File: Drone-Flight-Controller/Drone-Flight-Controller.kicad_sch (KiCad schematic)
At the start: 60 parts, among them J1 Screw_Terminal_01x02, J10 TestPoint, J2 Raspberry_Pi_4, J3 USB_B_Micro, J4 Conn_ARM_SWD_TagConnect_TC203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, J5 TestPoint, J6 TestPoint, J7 TestPoint, J8 TestPoint, J9 TestPoint, U1 LMR51430, U2 USBLC6-2SC6, U3 MPU-9150, U4 BMP280, U5 STM32F413ZHTx, U6 XTSD08G, Y1 16MHz

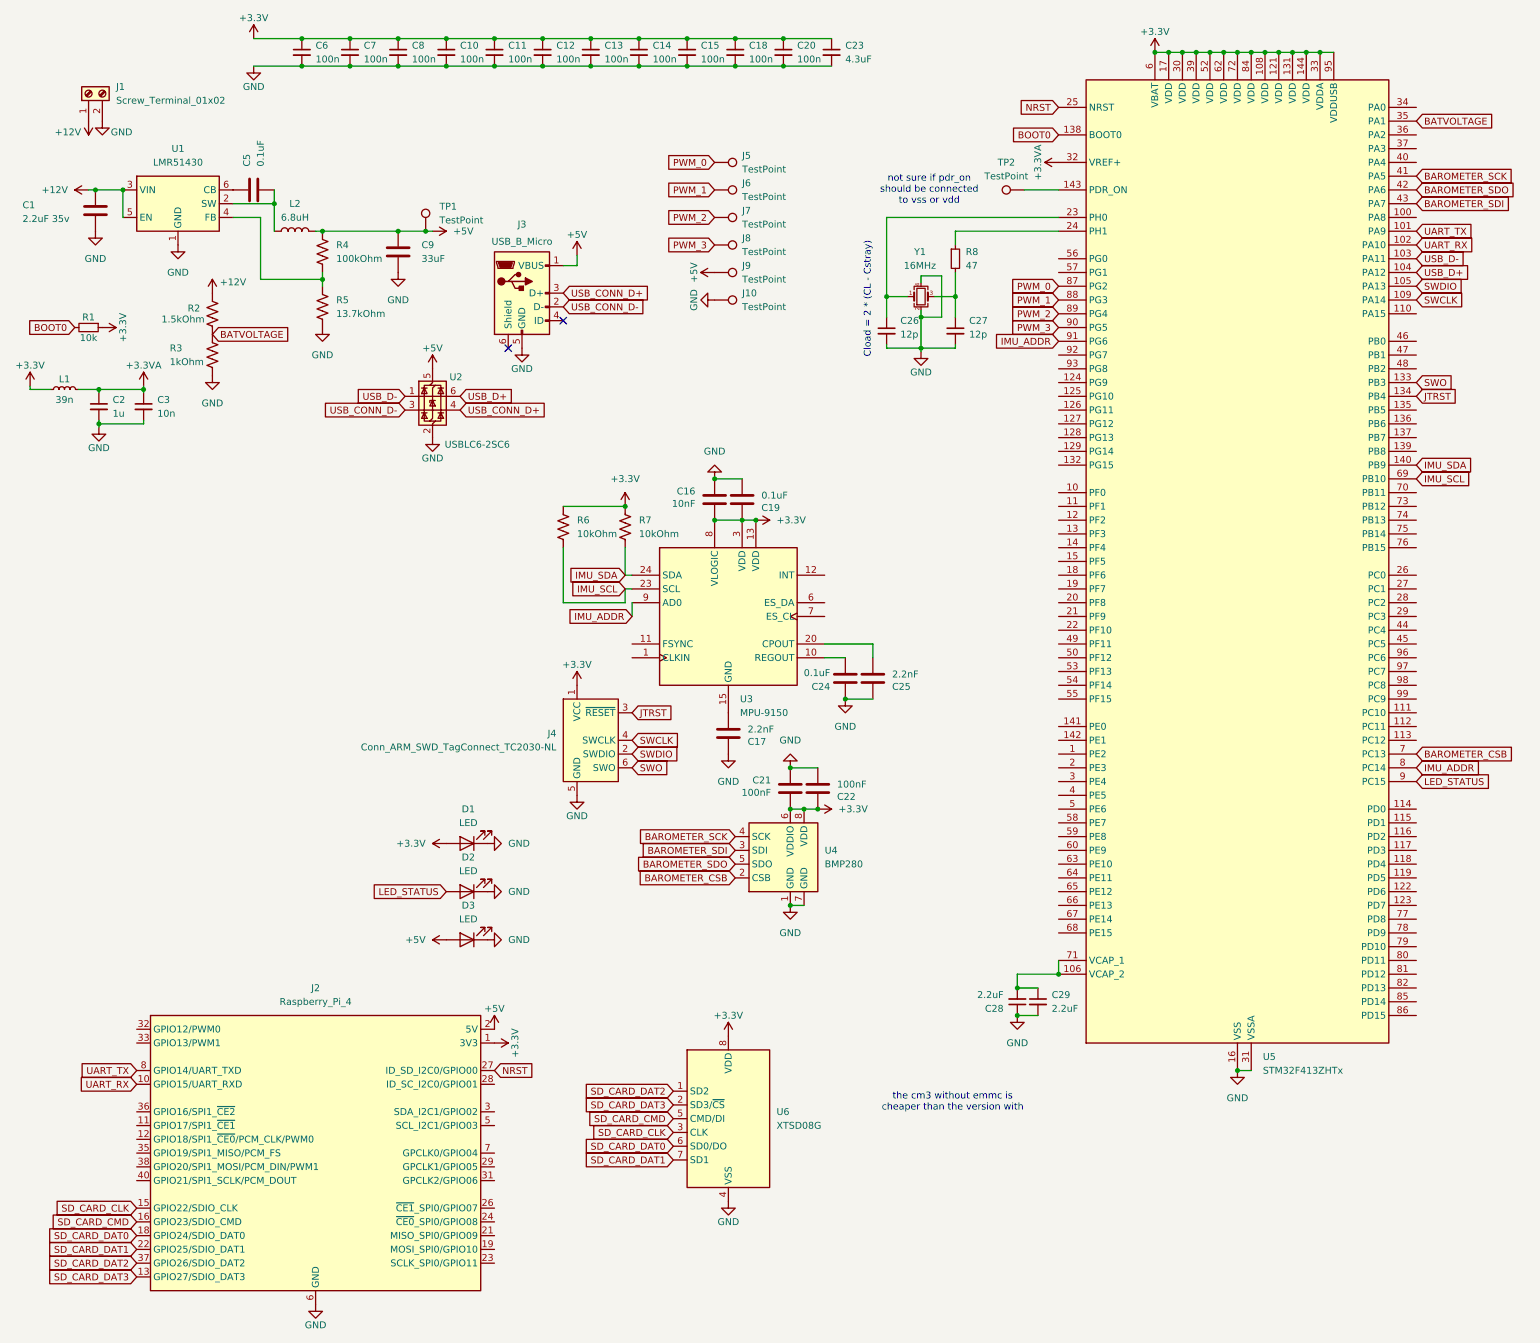
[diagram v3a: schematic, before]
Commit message: remove stm32
processing will be done on the rpi now
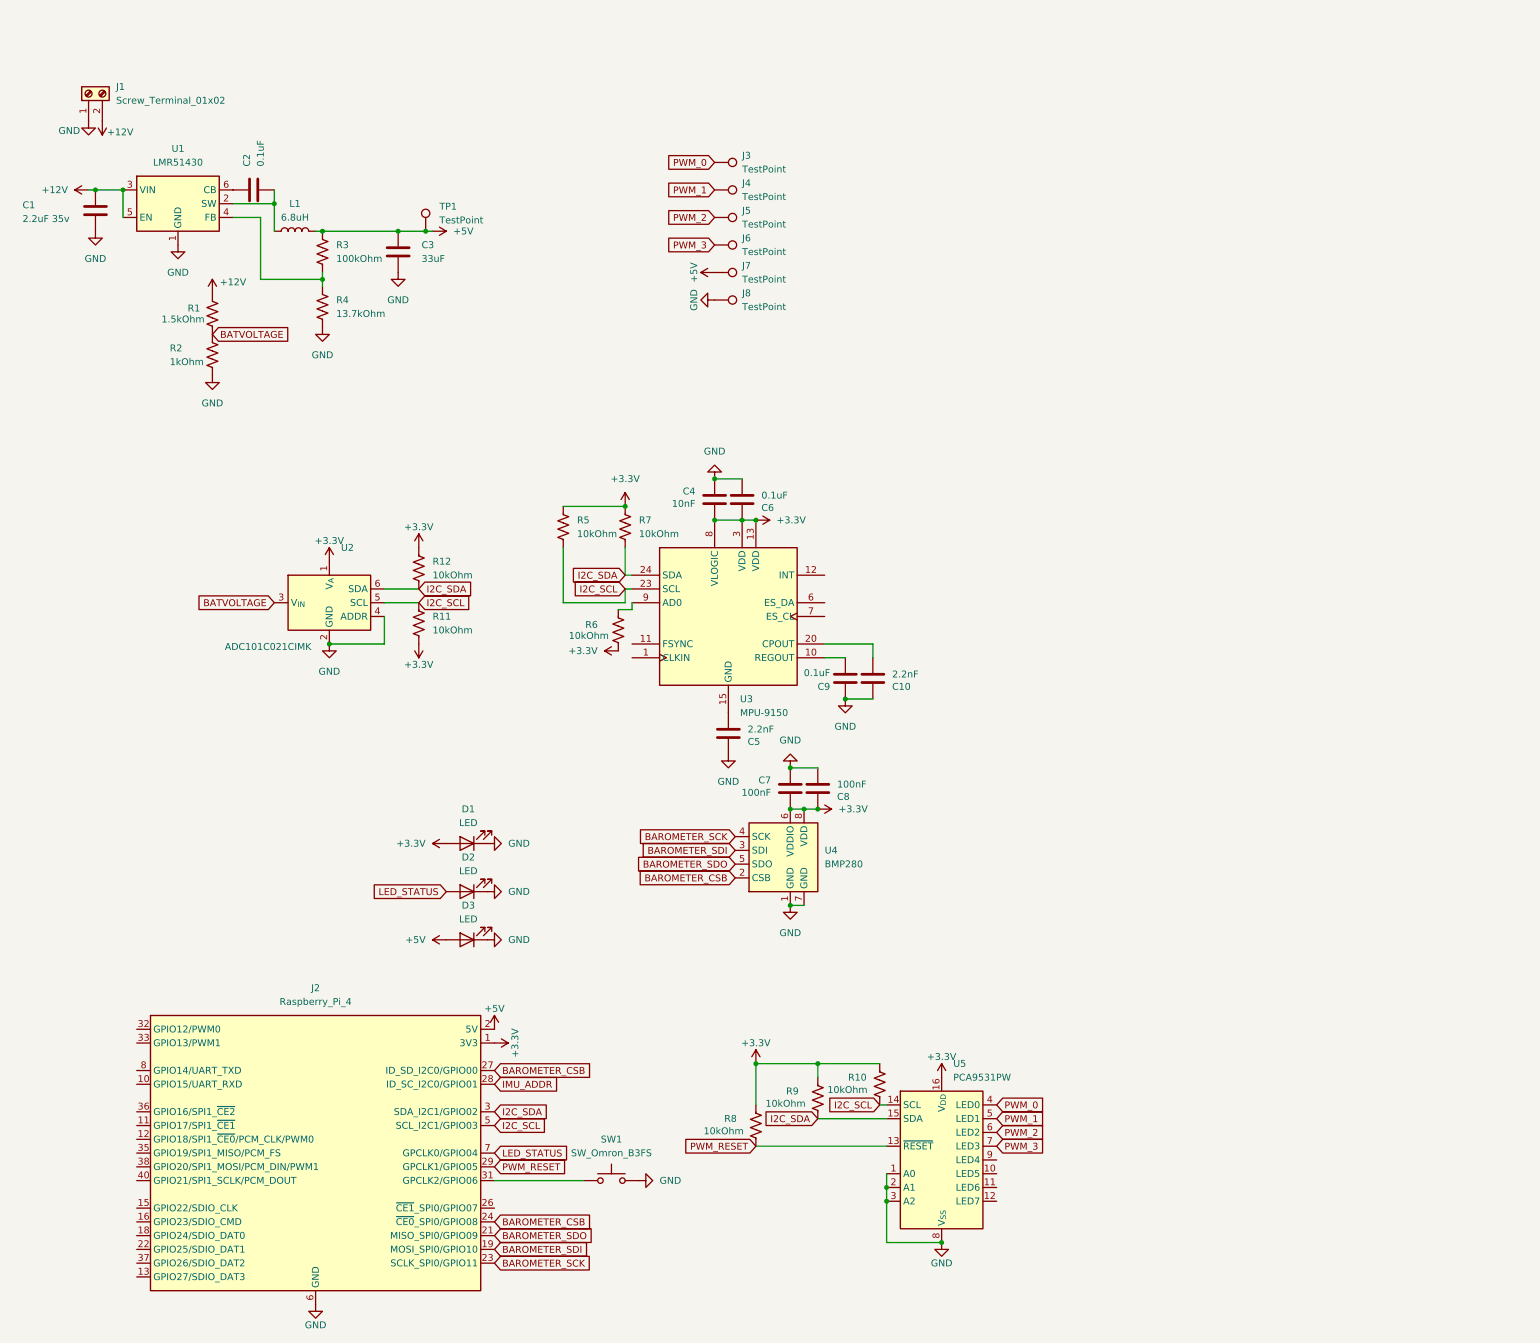
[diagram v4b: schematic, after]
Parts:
- removed C10, C11, C12, C13, C14, C15, C18, C20, C6, C7, C8: 100n, Capacitor_SMD:C_0402_1005Metric, symbol Device:C_Small
- removed C2: 1u, Capacitor_SMD:C_0402_1005Metric, symbol Device:C_Small
- removed C23: 4.3uF, Capacitor_SMD:C_0402_1005Metric, symbol Device:C_Small
- removed C26, C27: 12p, Capacitor_SMD:C_0402_1005Metric, symbol Device:C_Small
- removed C28, C29: 2.2uF, Capacitor_SMD:C_0402_1005Metric, symbol Device:C_Small
- removed C3: 10n, Capacitor_SMD:C_0402_1005Metric, symbol Device:C_Small
- removed J3: USB_B_Micro, Connector_USB:USB_Mini-B_Lumberg_2486_01_Horizontal, symbol Connector:USB_B_Micro
- removed J4: Conn_ARM_SWD_TagConnect_TC2030-NL, Connector:Tag-Connect_TC2030-IDC-NL_2x03_P1.27mm_Vertical, symbol Connector:Conn_ARM_SWD_TagConnect_TC2030-NL
- removed L1: 39n, Inductor_SMD:L_0402_1005Metric, symbol Device:L_Small
- removed R1: 10k, Resistor_SMD:R_0402_1005Metric, symbol Device:R_Small
- removed R8: 47, Resistor_SMD:R_0402_1005Metric, symbol Device:R_Small
- removed TP2: TestPoint, TestPoint:TestPoint_Pad_D1.0mm, symbol Connector:TestPoint
- removed U2: USBLC6-2SC6, Package_TO_SOT_SMD:SOT-23-6, symbol Power_Protection:USBLC6-2SC6
- removed U5: STM32F413ZHTx, Package_QFP:LQFP-144_20x20mm_P0.5mm, symbol MCU_ST_STM32F4:STM32F413ZHTx
- removed U6: XTSD08G, Package_LGA:LGA-8_8x6mm_P1.27mm, symbol Memory_Flash:XTSD08G
- removed Y1: 16MHz, Crystal:Crystal_SMD_3225-4Pin_3.2x2.5mm, symbol Device:Crystal_GND24_Small
- added R10, R11, R12, R6, R8, R9: 10kOhm, Resistor_SMD:R_0402_1005Metric, symbol Device:R_US
- added SW1: SW_Omron_B3FS, Button_Switch_SMD:SW_SPST_Omron_B3FS-100xP, symbol Switch:SW_Omron_B3FS
- added U2: ADC101C021CIMK, Package_TO_SOT_SMD:SOT-23-6, symbol Analog_ADC:ADC101C021CIMK
- added U5: PCA9531PW, Package_SO:TSSOP-16_4.4x5mm_P0.65mm, symbol Driver_LED:PCA9531PW
- C3: renamed from C9; footprint Capacitor_SMD:C_0504_1310Metric -> Capacitor_SMD:C_Elec_5x5.4
- renumbered C25 to C10, C5 to C2, C16 to C4, C17 to C5, C19 to C6, C21 to C7, C22 to C8, C24 to C9, J5 to J3, J6 to J4, J7 to J5, J8 to J6, J9 to J7, J10 to J8, L2 to L1, R2 to R1, R3 to R2, R4 to R3, R5 to R4, R6 to R5
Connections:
- net IMU_SCL is gone; now on net I2C_SCL: R5.2, U3.23 (SCL)
- net IMU_SDA is gone; now on net I2C_SDA: R7.2, U3.24 (SDA)
- net NRST is gone; now on net BAROMETER_CSB: J2.27 (ID_SD_I2C0/GPIO00)
- net +12V: now also J1.2 (Pin_2); no longer J1.1 (Pin_1)
- net +3.3V: now also R10.1, R11.2, R12.1, R6.2, R8.1, R9.1, U2.1 (V_{A}), U5.16 (V_{DD})
- net BAROMETER_CSB: now also J2.24 (~{CE0}_SPI0/GPIO08)
- net BAROMETER_SCK: now also J2.23 (SCLK_SPI0/GPIO11)
- net BAROMETER_SDI: now also J2.19 (MOSI_SPI0/GPIO10)
- net BAROMETER_SDO: now also J2.21 (MISO_SPI0/GPIO09)
- net BATVOLTAGE: now also U2.3 (V_{IN})
- net GND: now also J1.1 (Pin_1), SW1.2, U2.2 (GND), U2.4 (ADDR), U5.1 (A0), U5.2 (A1), U5.3 (A2), U5.8 (V_{SS}); no longer J1.2 (Pin_2)
- net IMU_ADDR: now also J2.28 (ID_SC_I2C0/GPIO01); no longer U3.9 (AD0)
- net LED_STATUS: now also J2.7 (GPCLK0/GPIO04)
- net PWM_0: now also U5.4 (LED0)
- net PWM_1: now also U5.5 (LED1)
- net PWM_2: now also U5.6 (LED2)
- net PWM_3: now also U5.7 (LED3)
- net PWM_RESET: now reaches J2.29 (GPCLK1/GPIO05)
- net PWM_RESET: now also R8.2, U5.13 (~{RESET})
- net I2C_SDA: now reaches J2.3 (SDA_I2C1/GPIO02)
- net I2C_SDA: now also R12.2, R9.2, U2.6 (SDA), U5.15 (SDA)
- net at J2.31 (GPCLK2/GPIO06): now also SW1.1
- net I2C_SCL: now reaches J2.5 (SCL_I2C1/GPIO03)
- net I2C_SCL: now also R10.2, R11.1, U2.5 (SCL), U5.14 (SCL)
- net SD_CARD_CLK: no longer names the net of J2.15 (GPIO22/SDIO_CLK)
- net SD_CARD_CMD: no longer names the net of J2.16 (GPIO23/SDIO_CMD)
- net SD_CARD_DAT0: no longer names the net of J2.18 (GPIO24/SDIO_DAT0)
- net SD_CARD_DAT1: no longer names the net of J2.22 (GPIO25/SDIO_DAT1)
- net SD_CARD_DAT2: no longer names the net of J2.37 (GPIO26/SDIO_DAT2)
- net SD_CARD_DAT3: no longer names the net of J2.13 (GPIO27/SDIO_DAT3)
- net UART_RX: no longer names the net of J2.10 (GPIO15/UART_RXD)
- net UART_TX: no longer names the net of J2.8 (GPIO14/UART_TXD)
- new net: R6.1, U3.9 (AD0)
- no-connect marks 2 -> 0
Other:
- note removed: "Cload = 2 * (CL - Cstray)"
- note removed: "not sure if pdr_on should be connected to vss or vdd"
- note removed: "the cm3 without emmc is cheaper than the version with"

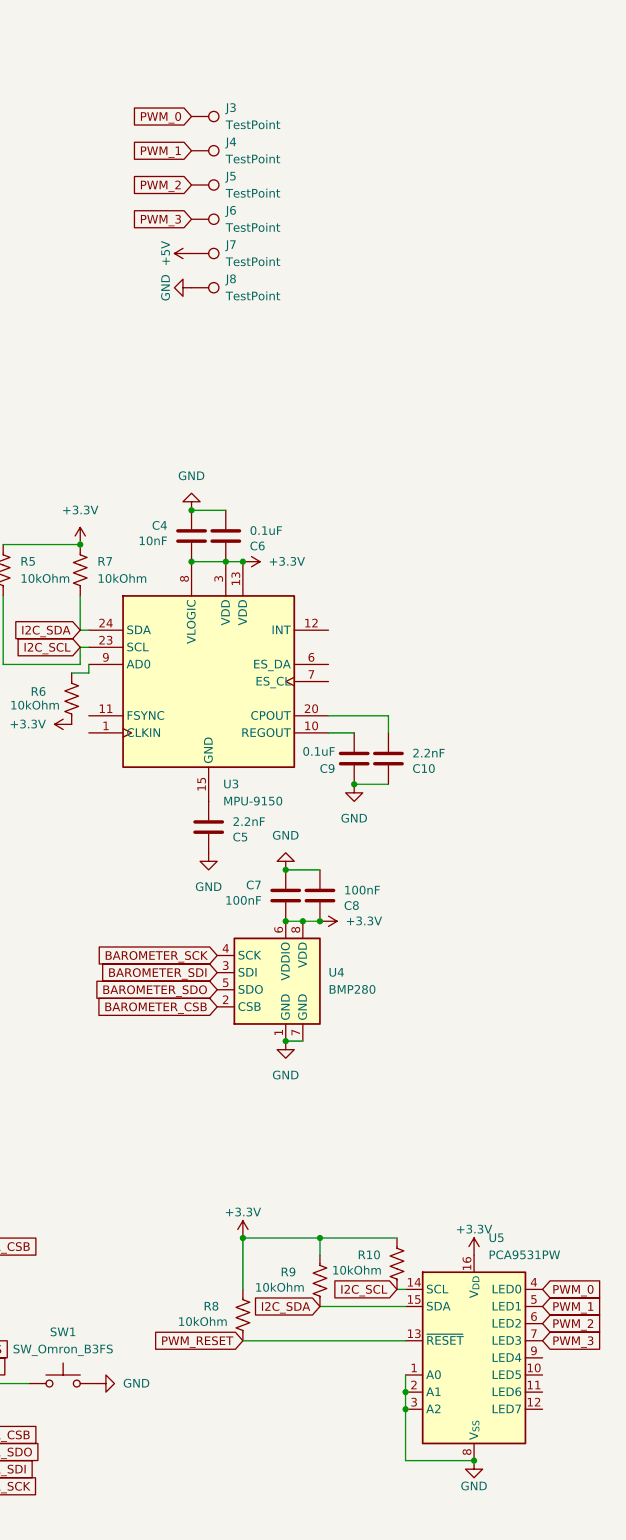
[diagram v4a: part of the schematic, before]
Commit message: pin header is female and on the bottom now
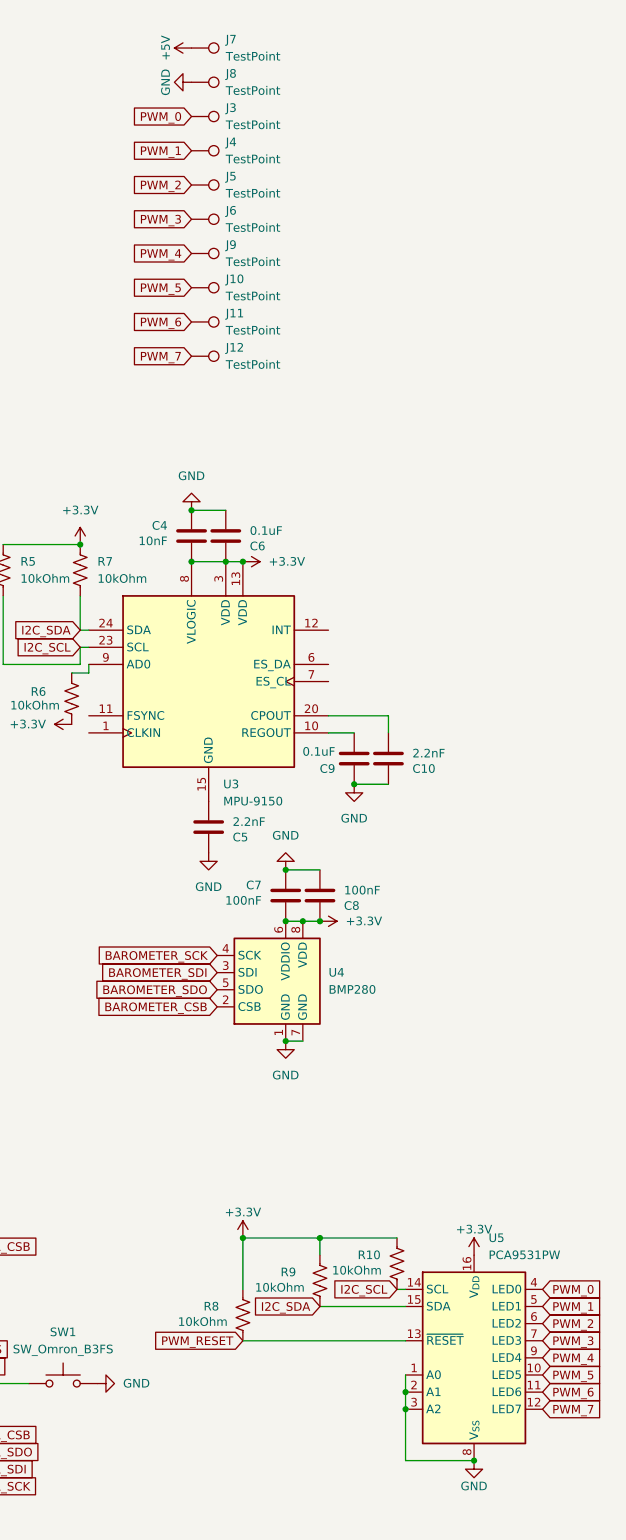
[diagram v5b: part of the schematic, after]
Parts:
- added J10, J11, J12, J9: TestPoint, TestPoint:TestPoint_Pad_D2.0mm, symbol Connector:TestPoint
- J2: footprint Connector_PinHeader_2.54mm:PinHeader_2x20_P2.54mm_Vertical -> Connector_PinSocket_2.54mm:PinSocket_2x20_P2.54mm_Vertical
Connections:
- net PWM_5: now reaches U5.10 (LED5)
- net PWM_5: now also J10.1
- net PWM_6: now reaches U5.11 (LED6)
- net PWM_6: now also J11.1
- net PWM_7: now reaches U5.12 (LED7)
- net PWM_7: now also J12.1
- net PWM_4: now reaches U5.9 (LED4)
- net PWM_4: now also J9.1
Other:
- moved on the sheet: J7, J8
